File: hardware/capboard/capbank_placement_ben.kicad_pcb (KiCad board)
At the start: 2 copper layers, 100 x 40 mm, 31 parts, among them SW1 SW_Push_1TS009xxxx-xxxx-xxxx_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, U1 HT7550-1, U2 MT3608

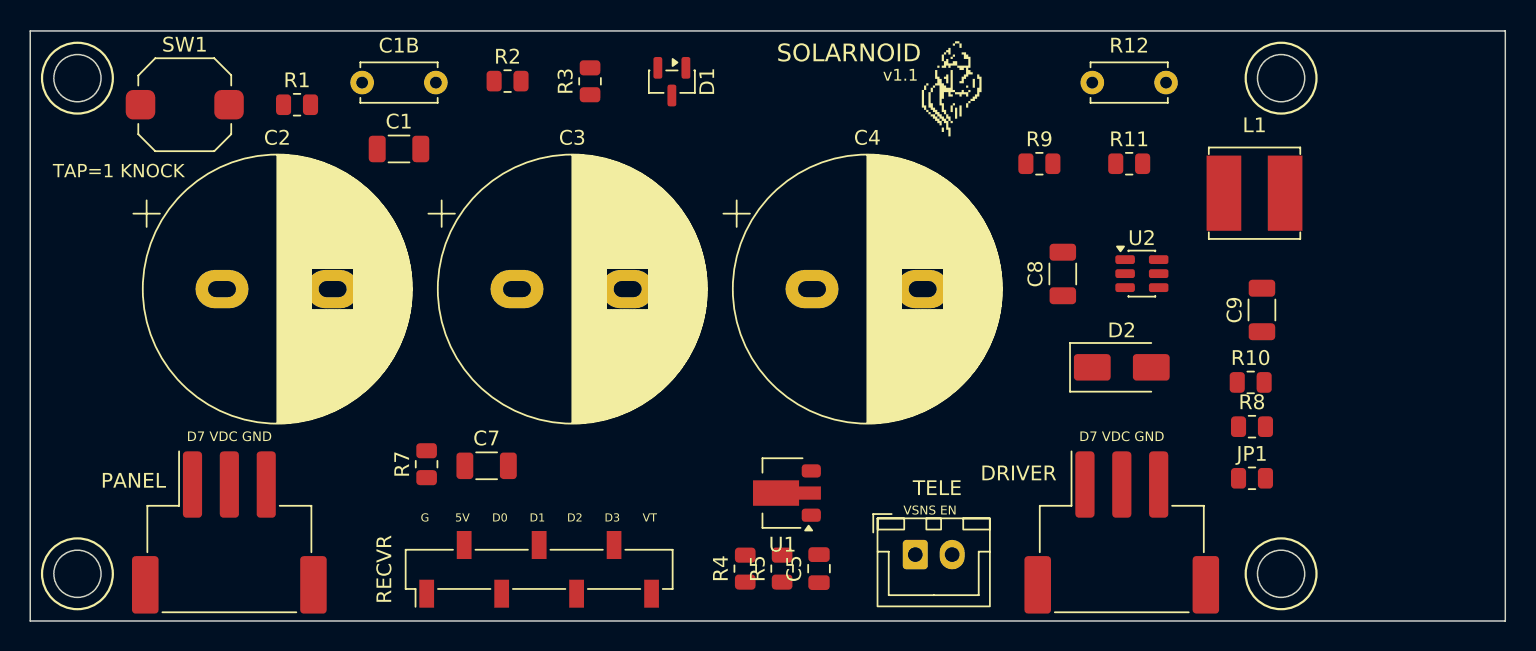
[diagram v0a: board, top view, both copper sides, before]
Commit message: hardware/capboard: v1.1 DRC-CLEAN -- 0 violations, 0 unconnected
Ben's spread-out placement + route_capboard.py. The router loads his placement
and adds only tracks, so his positions and silkscreen are authoritative and the
routing is reproducible after any re-arrangement.

Co-Authored-By: Claude Fable 5 <noreply@anthropic.com>
Claude-Session: https://claude.ai/code/session_01XEHUfVFPdvg3k1kXt9D9MK
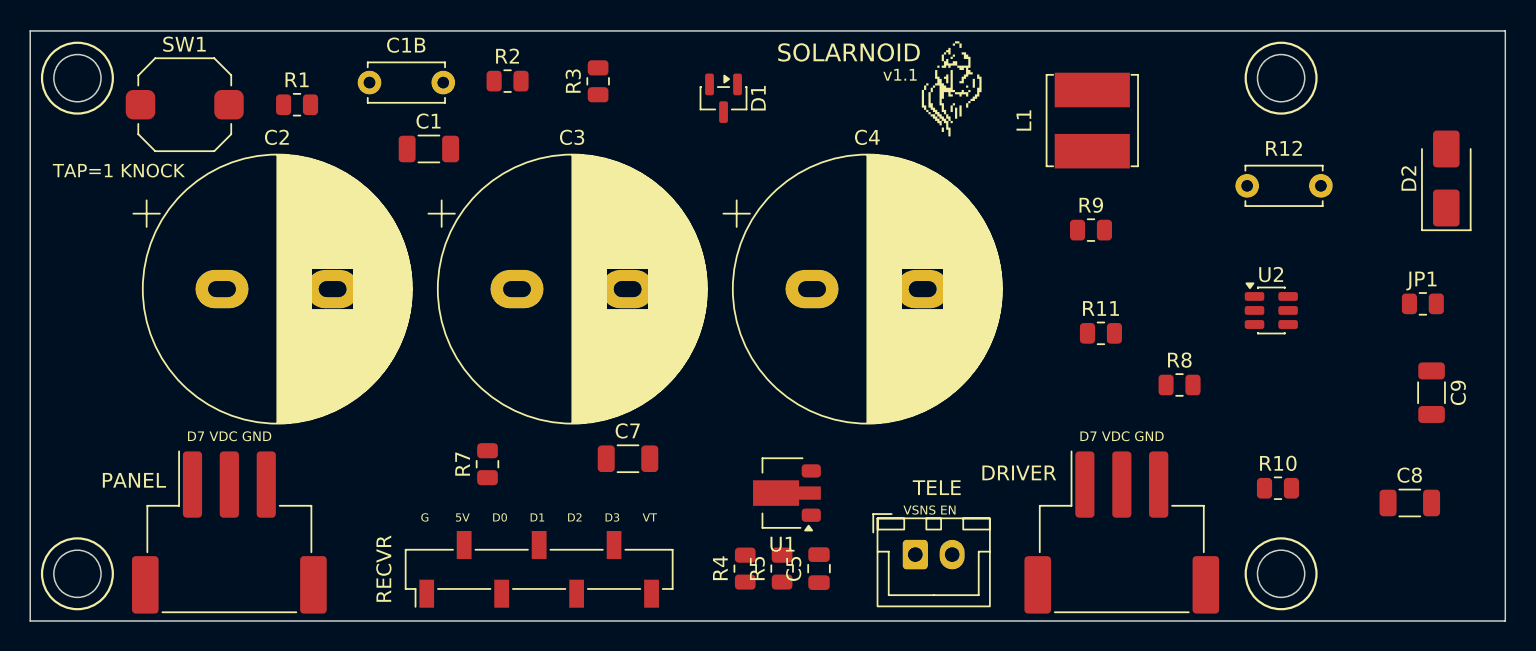
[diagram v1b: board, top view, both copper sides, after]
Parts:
- moved C8 28.2 mm to (93.5, 32.0), turned to 0 degrees
- moved D2 25.5 mm to (96.0, 10.0), turned to 90 degrees
- moved JP1 16.6 mm to (94.4, 18.5)
- moved C9 12.8 mm to (95.0, 24.5), turned to -90 degrees
- moved R12 12.6 mm to (82.5, 10.5)
- moved L1 12.1 mm to (72.0, 6.08), turned to 90 degrees
- moved R11 11.7 mm to (72.6, 20.5)
- moved C7 9.60 mm to (40.5, 29.0)
- moved U2 9.12 mm to (84.1, 18.9)
- moved R10 7.41 mm to (84.6, 31.0)
- moved R9 5.70 mm to (71.9, 13.5)
- moved R8 5.67 mm to (77.9, 24.0)
- moved R7 4.13 mm to (31.0, 29.4)
- moved D1 3.68 mm to (47.0, 4.56)
- moved C1 2.02 mm to (27.0, 8.00)
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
